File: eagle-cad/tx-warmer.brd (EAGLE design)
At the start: 44.5 x 44.5 mm, 22 parts

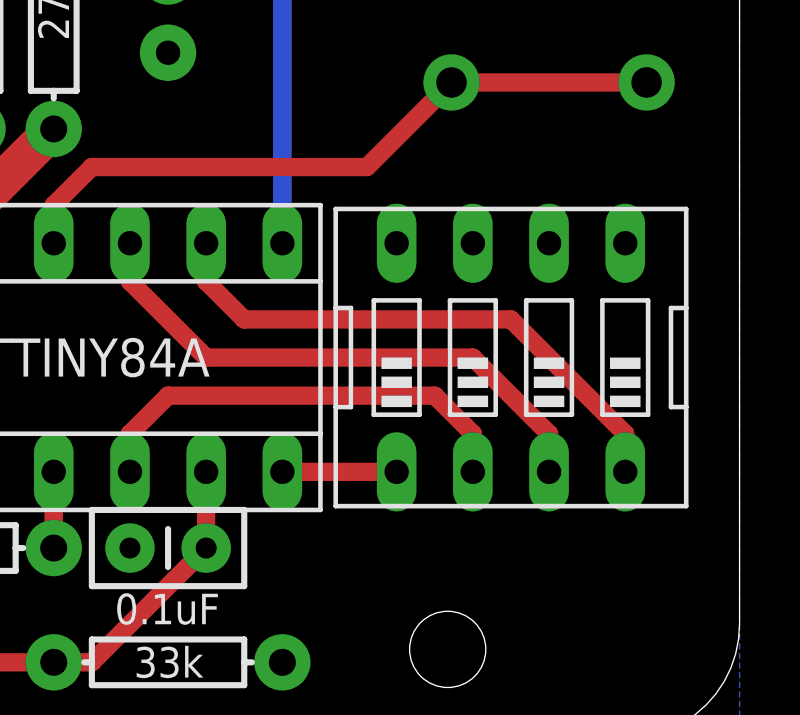
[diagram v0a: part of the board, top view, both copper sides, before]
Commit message: Flipped DIP-switches
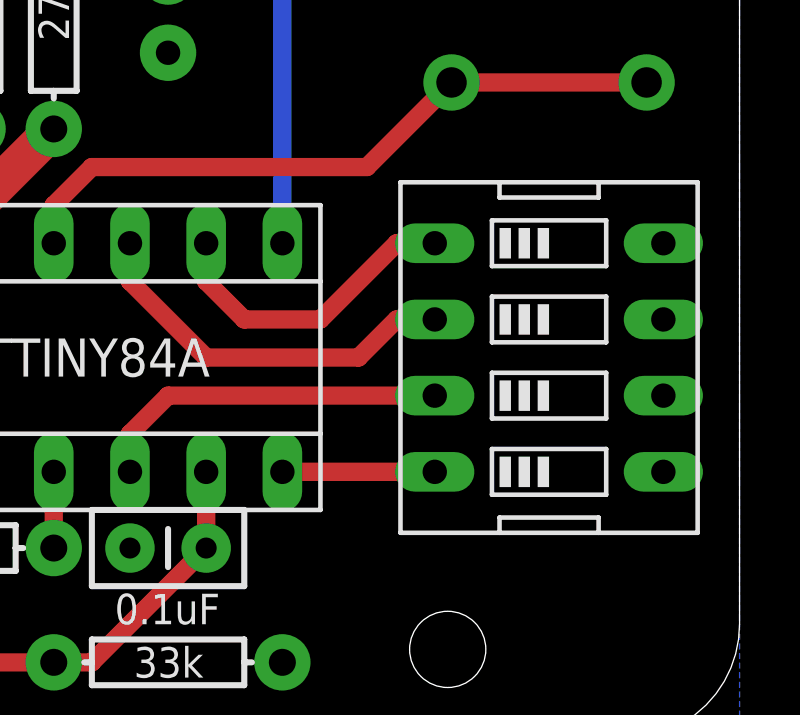
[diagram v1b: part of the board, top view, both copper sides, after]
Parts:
- moved SW1 1.27 mm to (36.8, 11.4), turned to 270 degrees
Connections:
- net N$1: now also SW1.4; no longer SW1.1
- net N$2: now also SW1.3; no longer SW1.2
- net N$20: now also SW1.1; no longer SW1.4
- net N$5: now also SW1.2; no longer SW1.3
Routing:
- net N$20: track 18.6 -> 10.5 mm
- net N$5: track 18.6 -> 13.0 mm
- net N$2: track 15.0 -> 12.0 mm
- net N$1: track 3.81 -> 5.08 mm
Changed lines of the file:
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@@
 <hole x="8.4582" y="40.2082" drill="2.54"/>
 <hole x="33.4518" y="1.7018" drill="2.54"/>
-<text x="19.05" y="13.335" size="1.27" layer="22" rot="MR180">TX-warmer v1.6</text>
-<text x="16.51" y="10.795" size="1.27" layer="22" rot="MR180">Pertti Erkkilä 2013</text>
+<text x="13.97" y="13.335" size="1.27" layer="22" rot="MR180">TX-warmer v1.6</text>
+<text x="11.43" y="10.795" size="1.27" layer="22" rot="MR180">Pertti Erkkilä 2013</text>
 <wire x1="8.89" y1="25.4" x2="3.81" y2="25.4" width="0.254" layer="21" curve="-106.260205"/>
 </plain>
@@
 <attribute name="VALUE" x="2.54" y="23.495" size="1.27" layer="27"/>
 </element>
-<element name="SW1" library="special" package="EDG-04" value="" x="35.56" y="11.43" smashed="yes">
-<attribute name="VALUE" x="29.718" y="4.826" size="1.27" layer="27" ratio="10"/>
+<element name="SW1" library="special" package="EDG-04" value="" x="36.83" y="11.43" smashed="yes" rot="R270">
+<attribute name="VALUE" x="30.226" y="17.272" size="1.27" layer="27" ratio="10" rot="R270"/>
 </element>
 </elements>
@@
 </signal>
 <signal name="N$1">
-<contactref element="SW1" pad="1"/>
 <contactref element="ATTINY84A" pad="7"/>
-<wire x1="31.75" y1="7.62" x2="27.94" y2="7.62" width="0.6096" layer="1"/>
+<contactref element="SW1" pad="4"/>
+<wire x1="33.02" y1="7.62" x2="27.94" y2="7.62" width="0.6096" layer="1"/>
 </signal>
 <signal name="N$2">
-<contactref element="SW1" pad="2"/>
 <contactref element="ATTINY84A" pad="5"/>
-<wire x1="34.29" y1="7.62" x2="34.29" y2="8.89" width="0.6096" layer="1"/>
-<wire x1="34.29" y1="8.89" x2="33.02" y2="10.16" width="0.6096" layer="1"/>
+<contactref element="SW1" pad="3"/>
 <wire x1="33.02" y1="10.16" x2="24.13" y2="10.16" width="0.6096" layer="1"/>
 <wire x1="24.13" y1="10.16" x2="22.86" y2="8.89" width="0.6096" layer="1"/>
@@
 </signal>
 <signal name="N$5">
-<contactref element="SW1" pad="3"/>
-<wire x1="36.83" y1="7.62" x2="36.83" y2="8.89" width="0.6096" layer="1"/>
-<wire x1="36.83" y1="8.89" x2="34.29" y2="11.43" width="0.6096" layer="1"/>
-<wire x1="34.29" y1="11.43" x2="25.4" y2="11.43" width="0.6096" layer="1"/>
 <contactref element="ATTINY84A" pad="10"/>
+<contactref element="SW1" pad="2"/>
+<wire x1="33.02" y1="12.7" x2="31.75" y2="12.7" width="0.6096" layer="1"/>
+<wire x1="31.75" y1="12.7" x2="30.48" y2="11.43" width="0.6096" layer="1"/>
+<wire x1="30.48" y1="11.43" x2="25.4" y2="11.43" width="0.6096" layer="1"/>
 <wire x1="25.4" y1="11.43" x2="22.86" y2="13.97" width="0.6096" layer="1"/>
 <wire x1="22.86" y1="13.97" x2="22.86" y2="15.24" width="0.6096" layer="1"/>
 </signal>
 <signal name="N$20">
-<contactref element="SW1" pad="4"/>
 <contactref element="ATTINY84A" pad="9"/>
-<wire x1="39.37" y1="7.62" x2="39.37" y2="8.89" width="0.6096" layer="1"/>
-<wire x1="39.37" y1="8.89" x2="35.56" y2="12.7" width="0.6096" layer="1"/>
-<wire x1="35.56" y1="12.7" x2="26.67" y2="12.7" width="0.6096" layer="1"/>
+<contactref element="SW1" pad="1"/>
+<wire x1="33.02" y1="15.24" x2="31.75" y2="15.24" width="0.6096" layer="1"/>
+<wire x1="31.75" y1="15.24" x2="29.21" y2="12.7" width="0.6096" layer="1"/>
+<wire x1="29.21" y1="12.7" x2="26.67" y2="12.7" width="0.6096" layer="1"/>
 <wire x1="26.67" y1="12.7" x2="25.4" y2="13.97" width="0.6096" layer="1"/>
 <wire x1="25.4" y1="13.97" x2="25.4" y2="15.24" width="0.6096" layer="1"/>

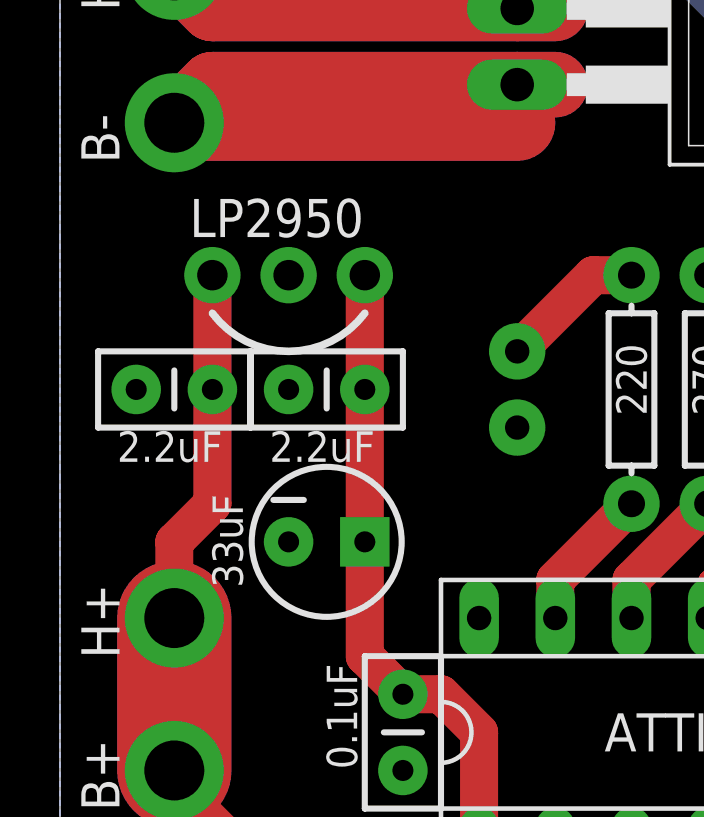
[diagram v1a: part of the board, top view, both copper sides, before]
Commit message: Changed capacitors near regulator from 0.1" to 0.2" spacing
To avoid confusion with 0.1uF caps and straight legs sit better at board.
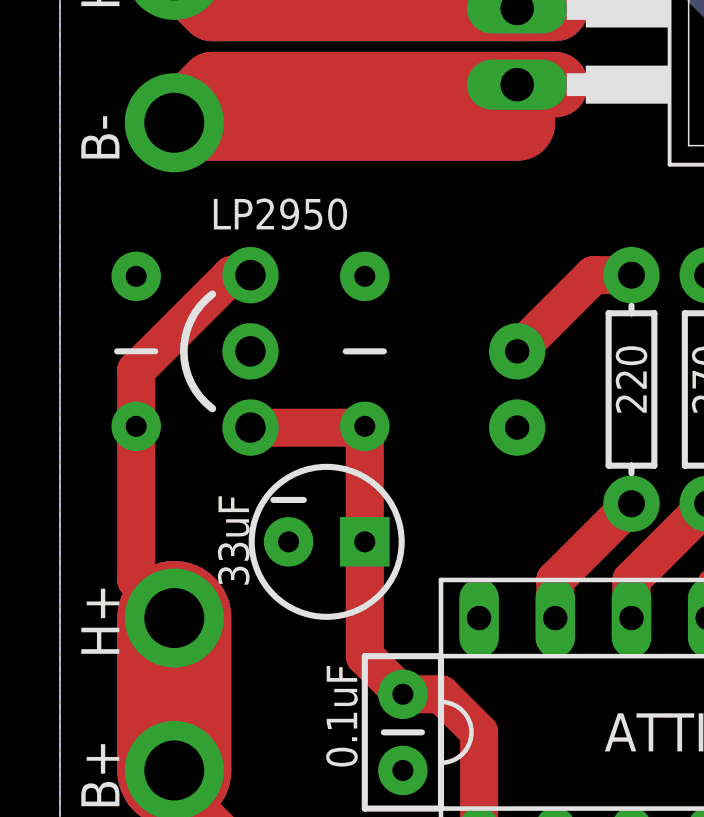
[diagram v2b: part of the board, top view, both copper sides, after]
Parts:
- C1, C2: device SparkFun-Passives:CAP-PTH-SMALLEZ -> SparkFun-Passives:CAP-PTH-5MM
- moved C2 2.84 mm to (1.27, 24.1), turned to 90 degrees
- moved LP2950 1.27 mm to (5.08, 26.7), turned to 270 degrees
- moved C1 1.27 mm to (8.89, 24.1), turned to 90 degrees
- renumbered C6 to C4
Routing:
- net N$4: track 33.6 -> 35.6 mm
- net 5V: track 23.9 -> 22.7 mm
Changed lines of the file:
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@@
 <text x="13.97" y="13.335" size="1.27" layer="22" rot="MR180">TX-warmer v1.6</text>
 <text x="11.43" y="10.795" size="1.27" layer="22" rot="MR180">Pertti Erkkilä 2013</text>
-<wire x1="8.89" y1="25.4" x2="3.81" y2="25.4" width="0.254" layer="21" curve="-106.260205"/>
+<wire x1="3.81" y1="22.225" x2="3.81" y2="26.035" width="0.254" layer="21" curve="-106.260205"/>
 </plain>
 <attributes>
@@
 </element>
 <element name="C5" library="SparkFun-Capacitors" package="CPOL-RADIAL-10UF-25V" value="33uF" x="7.62" y="17.78" smashed="yes">
-<attribute name="VALUE" x="4.826" y="16.256" size="1.016" layer="21" rot="R90"/>
-</element>
-<element name="C6" library="SparkFun-Passives" package="CAP-PTH-SMALLEZ" value="0.1uF" x="25.4" y="5.08" smashed="yes" rot="R180">
+<attribute name="VALUE" x="5.0292" y="16.256" size="1.016" layer="21" rot="R90"/>
+</element>
+<element name="C4" library="SparkFun-Passives" package="CAP-PTH-SMALLEZ" value="0.1uF" x="25.4" y="5.08" smashed="yes" rot="R180">
 <attribute name="VALUE" x="22.352" y="2.54" size="1.016" layer="21"/>
-</element>
-<element name="C1" library="SparkFun-Passives" package="CAP-PTH-SMALLEZ" value="2.2uF" x="8.89" y="22.86" smashed="yes" rot="R180">
-<attribute name="VALUE" x="5.715" y="20.447" size="1.016" layer="21"/>
-</element>
-<element name="C2" library="SparkFun-Passives" package="CAP-PTH-SMALLEZ" value="2.2uF" x="3.81" y="22.86" smashed="yes" rot="R180">
-<attribute name="VALUE" x="0.635" y="20.447" size="1.016" layer="21"/>
 </element>
 <element name="C3" library="SparkFun-Passives" package="CAP-PTH-SMALLEZ" value="0.1uF" x="10.16" y="12.7" smashed="yes" rot="R270">
@@
 <attribute name="NAME" x="0.7112" y="35.4838" size="1.27" layer="25" rot="R90"/>
 </element>
-<element name="LP2950" library="SparkFun-Connectors" package="1X03_NO_SILK" value="" x="3.81" y="26.67" smashed="yes">
-<attribute name="NAME" x="3.048" y="27.94" size="1.27" layer="25" ratio="10"/>
-<attribute name="VALUE" x="2.54" y="23.495" size="1.27" layer="27"/>
+<element name="LP2950" library="SparkFun-Connectors" package="1X03_NO_SILK" value="" x="5.08" y="26.67" smashed="yes" rot="R270">
+<attribute name="NAME" x="8.382" y="29.21" size="1.016" layer="25" ratio="10" rot="R180"/>
+<attribute name="VALUE" x="1.905" y="27.94" size="1.27" layer="27" rot="R270"/>
 </element>
 <element name="SW1" library="special" package="EDG-04" value="" x="36.83" y="11.43" smashed="yes" rot="R270">
 <attribute name="VALUE" x="30.226" y="17.272" size="1.27" layer="27" ratio="10" rot="R270"/>
+</element>
+<element name="C2" library="SparkFun-Passives" package="CAP-PTH-5MM" value="2.2uF" x="1.27" y="24.13" smashed="yes" rot="R90">
+<attribute name="VALUE" x="0.508" y="22.479" size="1.016" layer="27" rot="R90"/>
+</element>
+<element name="C1" library="SparkFun-Passives" package="CAP-PTH-5MM" value="2.2uF" x="8.89" y="24.13" smashed="yes" rot="R90">
+<attribute name="VALUE" x="8.128" y="22.479" size="1.016" layer="27" rot="R90"/>
 </element>
 </elements>
@@
 <signal name="N$4">
 <contactref element="R3" pad="P$1"/>
-<contactref element="C2" pad="1"/>
 <contactref element="B+" pad="1"/>
 <contactref element="H+" pad="1"/>
@@
 <wire x1="2.54" y1="10.16" x2="2.54" y2="15.24" width="3.81" layer="1"/>
 <contactref element="LP2950" pad="1"/>
-<wire x1="3.81" y1="22.86" x2="3.81" y2="26.67" width="1.27" layer="1"/>
 <wire x1="8.89" y1="1.27" x2="8.89" y2="3.81" width="0.6096" layer="1"/>
 <wire x1="8.89" y1="3.81" x2="2.54" y2="10.16" width="0.6096" layer="1"/>
-<wire x1="2.54" y1="15.24" x2="2.54" y2="17.78" width="1.27" layer="1"/>
-<wire x1="2.54" y1="17.78" x2="3.81" y2="19.05" width="1.27" layer="1"/>
-<wire x1="3.81" y1="19.05" x2="3.81" y2="22.86" width="1.27" layer="1"/>
+<contactref element="C2" pad="1"/>
+<wire x1="5.08" y1="26.67" x2="4.445" y2="26.67" width="1.27" layer="1"/>
+<wire x1="4.445" y1="26.67" x2="1.27" y2="23.495" width="1.27" layer="1"/>
+<wire x1="1.27" y1="23.495" x2="1.27" y2="21.63" width="1.27" layer="1"/>
+<wire x1="1.27" y1="21.63" x2="1.27" y2="16.51" width="1.27" layer="1"/>
+<wire x1="1.27" y1="16.51" x2="2.54" y2="15.24" width="1.27" layer="1"/>
 </signal>
 <signal name="GND">
@@
 <contactref element="LED1" pad="K"/>
 <contactref element="C5" pad="2"/>
-<contactref element="C6" pad="2"/>
-<contactref element="C1" pad="2"/>
-<contactref element="C2" pad="2"/>
+<contactref element="C4" pad="2"/>
 <contactref element="C3" pad="2"/>
 <polygon width="0.6096" layer="16" isolate="0.6096">
@@
 <contactref element="SW1" pad="6"/>
 <contactref element="SW1" pad="5"/>
+<contactref element="C2" pad="2"/>
+<contactref element="C1" pad="2"/>
 </signal>
 <signal name="5V">
 <contactref element="ATTINY84A" pad="1"/>
 <contactref element="C5" pad="1"/>
-<contactref element="C1" pad="1"/>
 <contactref element="C3" pad="1"/>
 <contactref element="R1" pad="P$1"/>
 <wire x1="12.7" y1="5.08" x2="12.7" y2="7.62" width="0.6096" layer="1"/>
 <contactref element="LP2950" pad="3"/>
-<wire x1="8.89" y1="22.86" x2="8.89" y2="26.67" width="1.27" layer="1"/>
-<wire x1="8.89" y1="17.78" x2="8.89" y2="22.86" width="1.27" layer="1"/>
 <wire x1="10.16" y1="12.7" x2="11.43" y2="12.7" width="1.27" layer="1"/>
 <wire x1="11.43" y1="12.7" x2="12.7" y2="11.43" width="1.27" layer="1"/>
@@
 <wire x1="8.89" y1="17.78" x2="8.89" y2="13.97" width="1.27" layer="1"/>
 <wire x1="8.89" y1="13.97" x2="10.16" y2="12.7" width="1.27" layer="1"/>
+<contactref element="C1" pad="1"/>
+<wire x1="5.08" y1="21.59" x2="8.89" y2="21.59" width="1.27" layer="1"/>
+<wire x1="8.89" y1="21.59" x2="8.89" y2="21.63" width="1.27" layer="1"/>
+<wire x1="8.89" y1="21.63" x2="8.89" y2="17.78" width="1.27" layer="1"/>
 </signal>
 <signal name="N$6">
@@
 <contactref element="ATTINY84A" pad="6"/>
 <wire x1="20.32" y1="1.27" x2="16.51" y2="1.27" width="0.6096" layer="1"/>
-<contactref element="C6" pad="1"/>
+<contactref element="C4" pad="1"/>
 <wire x1="20.32" y1="1.27" x2="21.59" y2="1.27" width="0.6096" layer="1"/>
 <wire x1="21.59" y1="1.27" x2="25.4" y2="5.08" width="0.6096" layer="1"/>

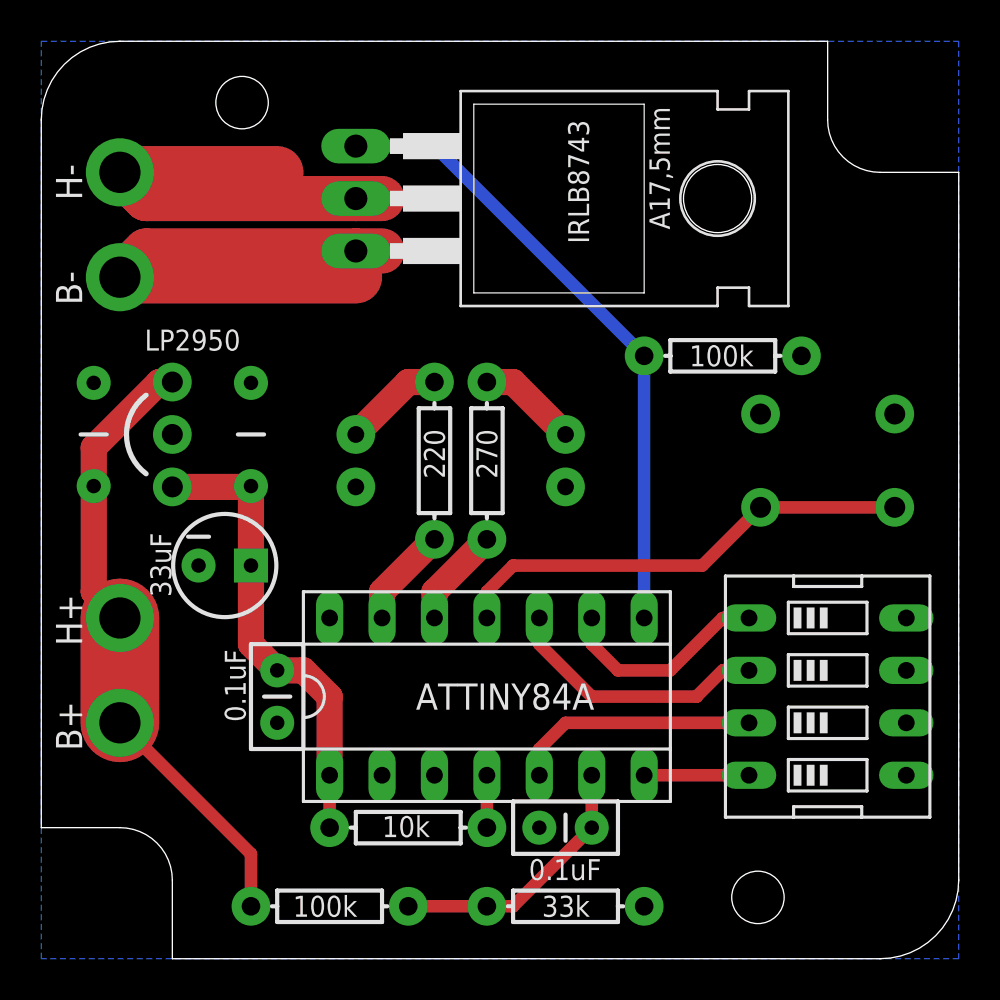
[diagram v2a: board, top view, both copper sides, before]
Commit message: Moved CPU a bit to make room for big cap
Fixed visibility of new caps.
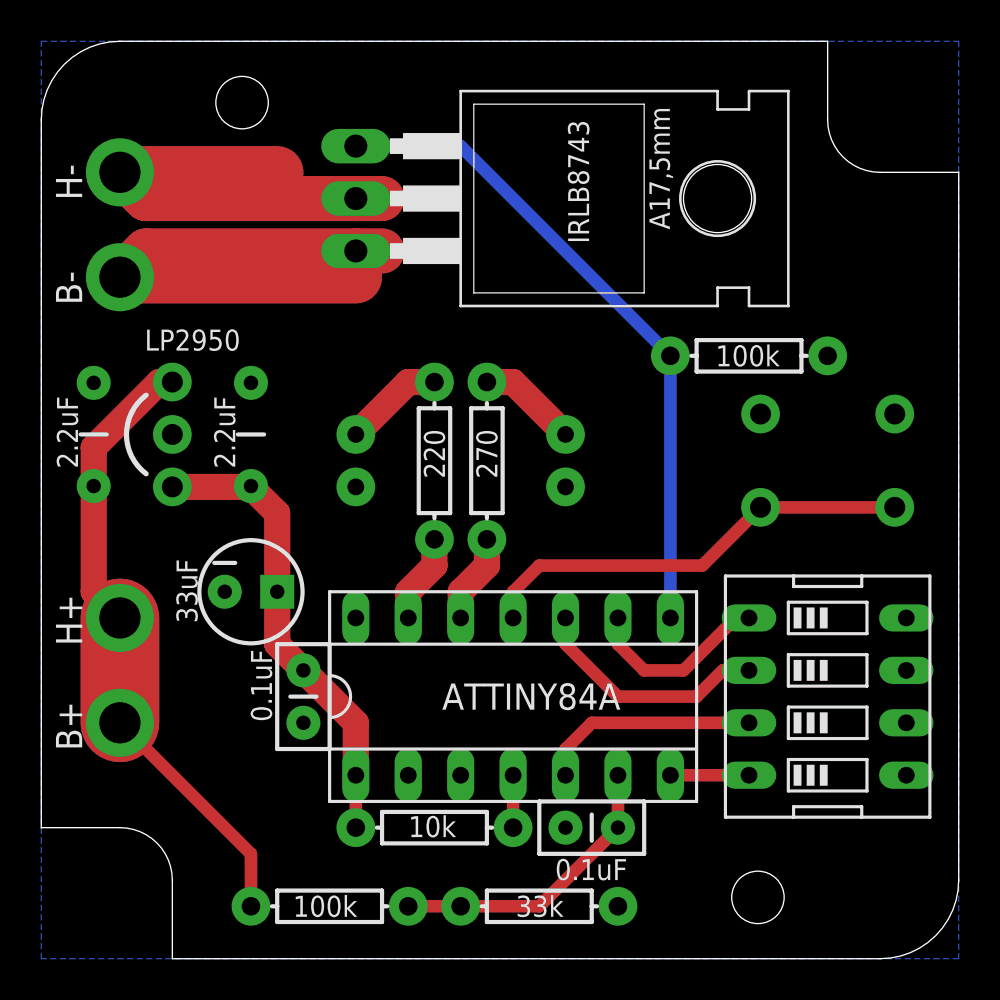
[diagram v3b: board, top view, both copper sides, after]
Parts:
- moved C5 1.80 mm to (8.89, 16.5)
- moved C4 1.27 mm to (26.7, 5.08)
- moved R6 1.27 mm to (33.0, 27.9)
- moved ATTINY84A 1.27 mm to (21.6, 11.4)
- moved C3 1.27 mm to (11.4, 12.7)
- moved R1 1.27 mm to (17.8, 5.08)
- moved R4 1.27 mm to (22.9, 1.27)
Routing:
- net N$13: track 22.7 -> 21.5 mm
- net N$5: track 13.0 -> 11.7 mm
- net N$20: track 10.5 -> 9.20 mm
- net N$7: track 13.0 -> 14.3 mm
- net N$2: track 12.0 -> 10.7 mm
- net N$1: track 5.08 -> 3.81 mm
- net N$6: track 30.9 -> 32.1 mm
- net N$18: track 4.86 -> 4.34 mm
- net N$12: track 4.86 -> 4.34 mm
